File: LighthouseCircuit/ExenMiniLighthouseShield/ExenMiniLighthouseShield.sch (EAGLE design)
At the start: 23 parts

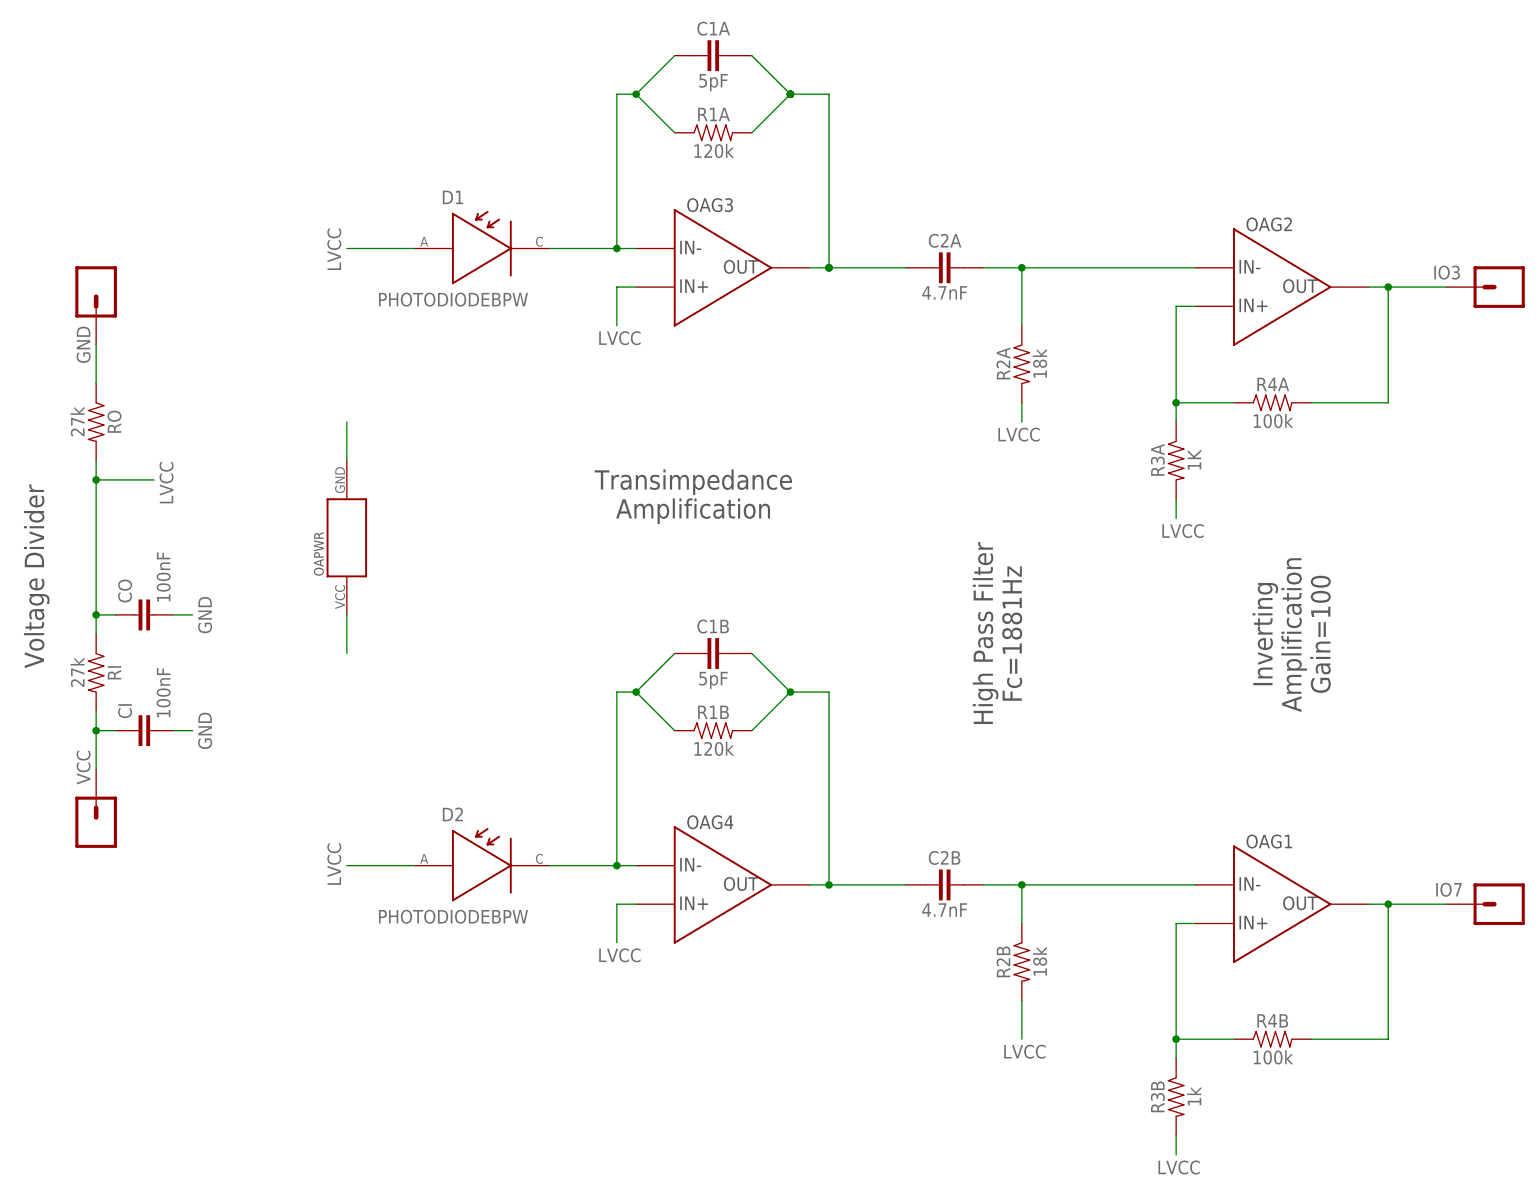
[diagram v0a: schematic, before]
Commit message: Moved to separate PID configuration for each wheel. Since the left wheel is offset toward the rear and the right wheel is offset toward the front, the left wheel needs to be less aggressive or the Zippy will turn more quickly to the right and will tilt the robot and pull the right wheel off the ground, preventing contact with the floor. On the other hand, the right wheel needs to be more aggressive or turns to the left will be slower than turns to the right.
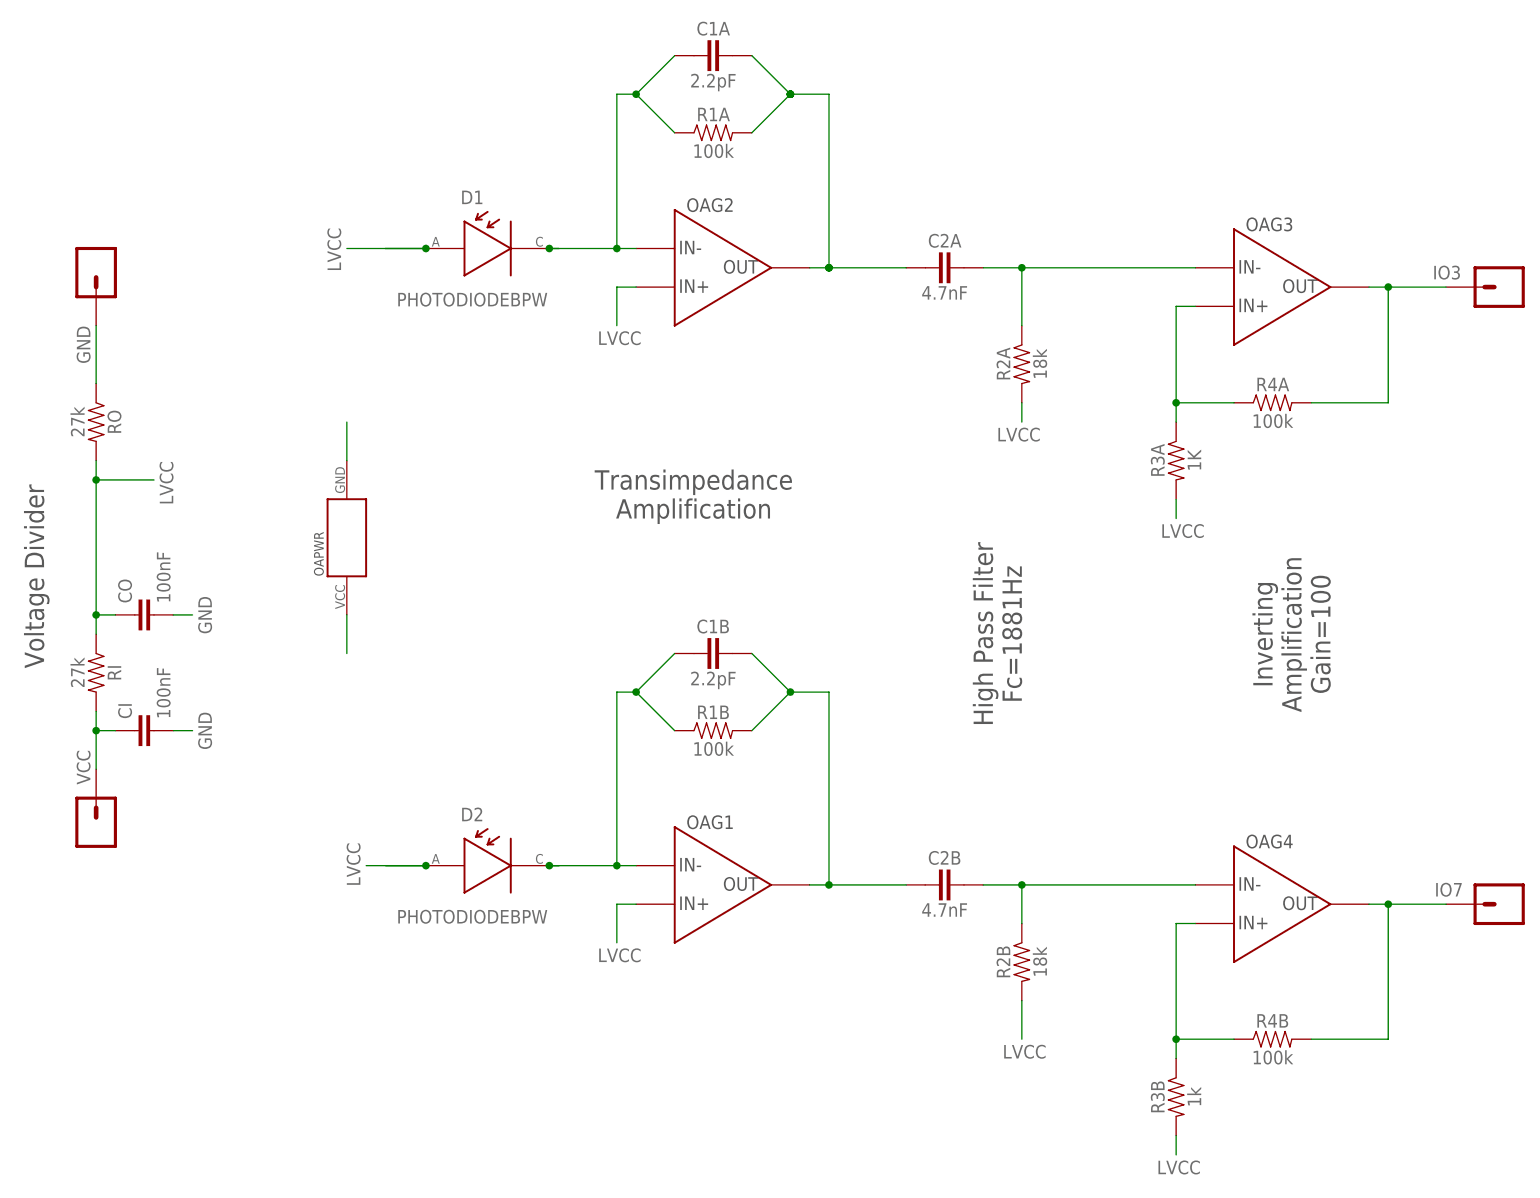
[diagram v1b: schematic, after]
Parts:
- C1A, C1B: value 5pF -> 2.2pF
- GND: value (none) -> SINGLE-THROUGH-HOLE; device SparkFun-Connectors:CONN_01PTH_NO_SILK_YES_STOP -> ZippyComponentLibrary:SINGLE-THROUGH-HOLE
- R1A, R1B: value 120k -> 100k
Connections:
- net D1IN: now also OAG1.IN-; no longer OAG4.IN-
- net D1OA2P: now also OAG4.IN-; no longer OAG1.IN-
- net D1OAOUT1: now also OAG1.OUT; no longer OAG4.OUT
- net D2IN: now also OAG2.IN-; no longer OAG3.IN-
- net D2OA1OUT: now also OAG2.OUT; no longer OAG3.OUT
- net D2OA2N: now also OAG3.IN+; no longer OAG2.IN+
- net D2OA2P: now also OAG3.IN-; no longer OAG2.IN-
- net IO3: now also OAG3.OUT; no longer OAG2.OUT
- net IO7: now also OAG4.OUT; no longer OAG1.OUT
- net LVCC: now also OAG1.IN+, OAG2.IN+; no longer OAG3.IN+, OAG4.IN+
- net N$11: now also OAG4.IN+; no longer OAG1.IN+
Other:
- moved on the sheet: D1, D2, OAG1, OAG2, OAG3, OAG4

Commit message: Zippies can now perform perfectly synchronous drive along any predefined path.
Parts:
- removed OA: TLV2464IDM, ZippyComponentLibrary:TLV2464IDM
- added U$1: TLV2464IPW, ZippyComponentLibrary:TLV2464IPW
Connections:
- net D1IN: now also U$1G1.IN-; no longer OAG1.IN-
- net D1OA2P: now also U$1G4.IN-; no longer OAG4.IN-
- net D1OAOUT1: now also U$1G1.OUT; no longer OAG1.OUT
- net D2IN: now also U$1G2.IN-; no longer OAG2.IN-
- net D2OA1OUT: now also U$1G2.OUT; no longer OAG2.OUT
- net D2OA2N: now also U$1G3.IN+; no longer OAG3.IN+
- net D2OA2P: now also U$1G3.IN-; no longer OAG3.IN-
- net GND: now also U$1PWR.GND; no longer OAPWR.GND
- net IO3: now also U$1G3.OUT; no longer OAG3.OUT
- net IO7: now also U$1G4.OUT; no longer OAG4.OUT
- net LVCC: now also U$1G1.IN+, U$1G2.IN+; no longer OAG1.IN+, OAG2.IN+
- net N$11: now also U$1G4.IN+; no longer OAG4.IN+
- net VCC: now also U$1PWR.VCC; no longer OAPWR.VCC
